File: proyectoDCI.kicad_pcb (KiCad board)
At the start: 2 copper layers, 45 x 20 mm, 27 parts, among them P1 CONN_02X04, P2 CONN_01X01, P3 GSG-RF-CONN, P4 GSG-RF-CONN, U1 AD5933, U2 ADG849, U3 AD8606, U4 ASFLMB-16.000MHZ-LY-T, U5 ADP150

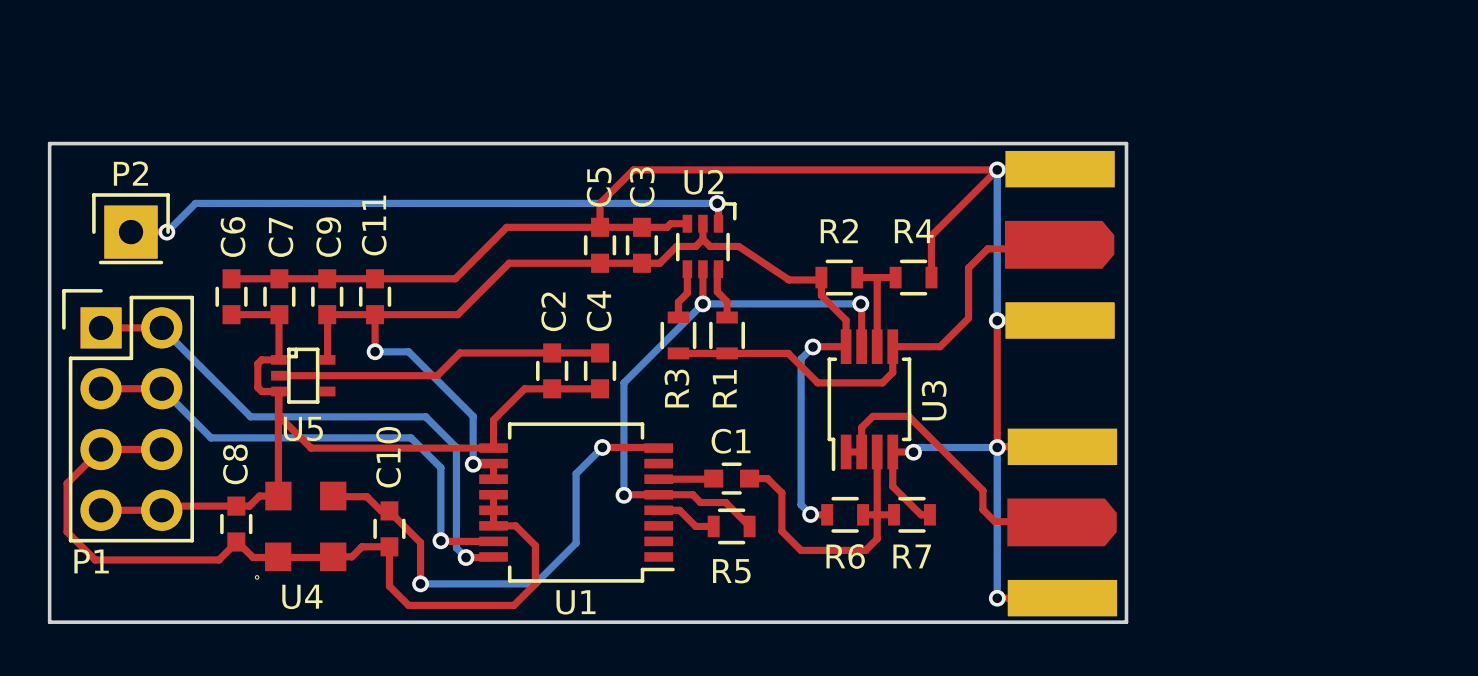
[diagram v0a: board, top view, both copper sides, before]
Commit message: Solucionados todos los problemas de DRC
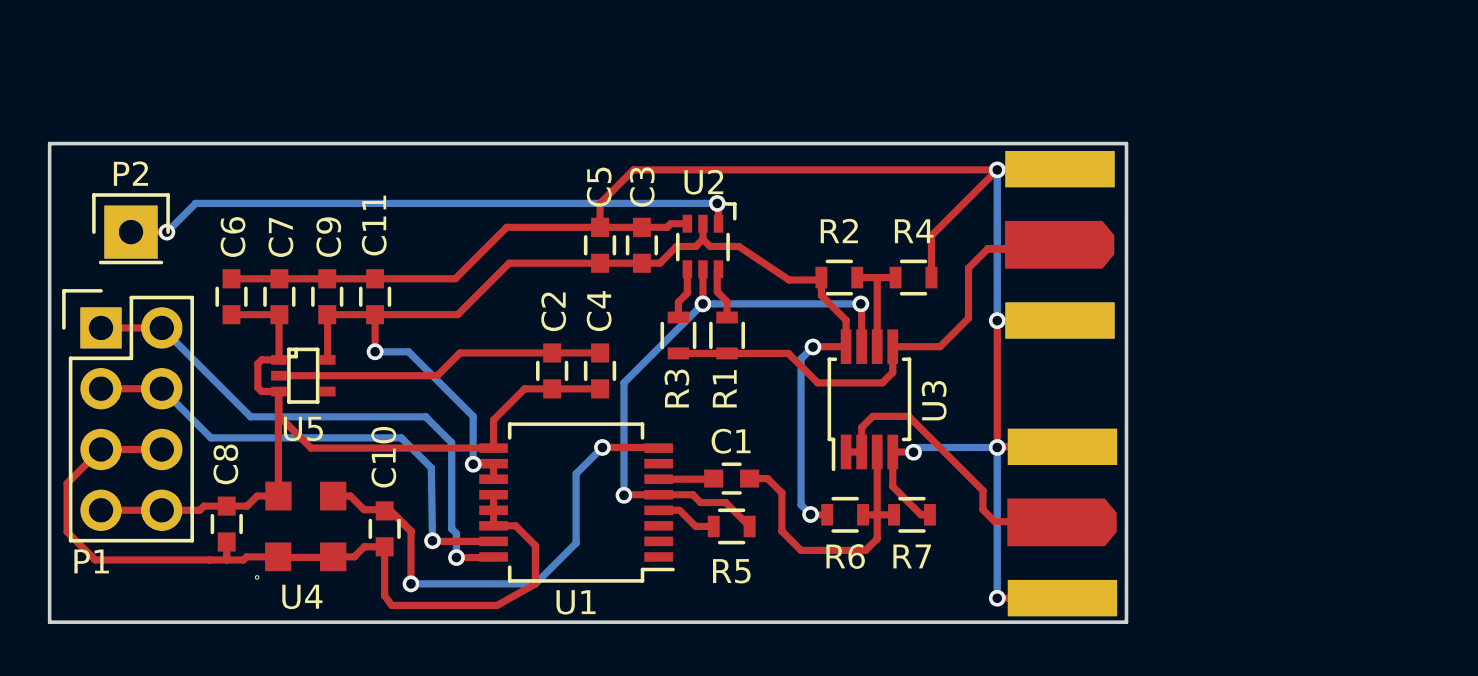
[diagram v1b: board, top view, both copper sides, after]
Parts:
- moved C8 0.40 mm to (157.4, 116.4)
- moved C10 0.20 mm to (164.0, 116.6)
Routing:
- net /Senal/CIN: track 20.6 -> 25.7 mm
- net /Senal/COUT: track 12.3 -> 14.6 mm
- net /Otros/MCLK: track 20.0 -> 22.1 mm
- added copper zone on B.Cu, net GND
- added copper zone on F.Cu, net GND

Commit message: Se agrego la silueta del TCXO y se corrigieron los footprints de los SMA
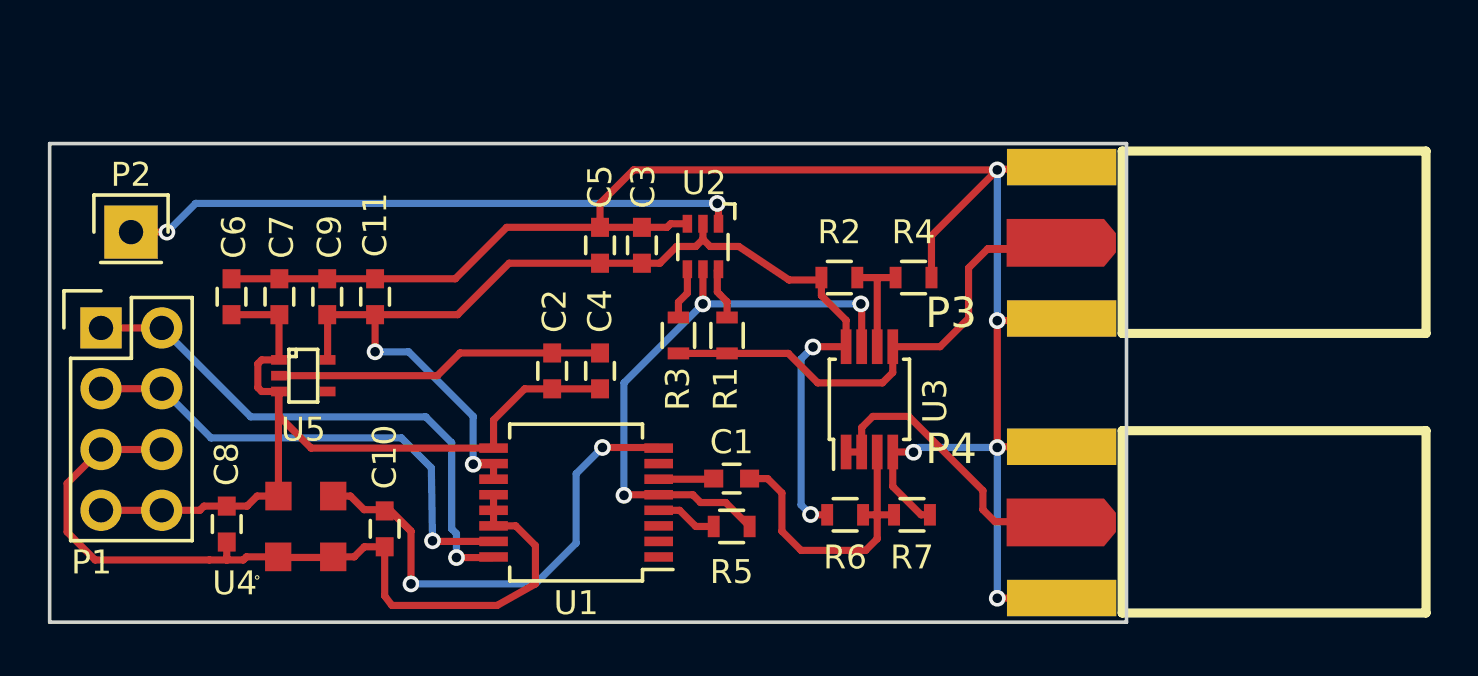
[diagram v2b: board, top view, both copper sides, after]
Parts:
- P3, P4: moved to F.Cu
- moved P3 2.62 mm to (201.2, 103.4)
- moved P4 2.54 mm to (201.2, 115.1)
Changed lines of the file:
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@@
   )
   (setup
-    (last_trace_width 0.3)
+    (last_trace_width 0.15)
     (user_trace_width 0.15)
     (user_trace_width 0.3)
@@
     (add_net VDD)
   )
+  (module SMA_EDGE:SMA_EDGE (layer F.Cu)
+    (at 201.168 115.062)
+    (fp_text reference P4 (at -13.5 -1.8) (layer F.SilkS)
+      (effects (font (thickness 0.3048)))
+    )
+    (fp_text value GSG-RF-CONN (at 0 2.54) (layer F.SilkS) hide
+      (effects (font (thickness 0.3048)))
+    )
+    (fp_line (start -6.35 -2.5654) (end -6.35 5.0546) (layer F.SilkS) (width 0.381))
+    (fp_line (start -6.35 5.0546) (end 6.35 5.0546) (layer F.SilkS) (width 0.381))
+    (fp_line (start 6.35 5.0546) (end 6.35 -2.5654) (layer F.SilkS) (width 0.381))
+    (fp_line (start 6.35 -2.5654) (end -6.35 -2.5654) (layer F.SilkS) (width 0.381))
+    (pad 0 connect rect (at -8.8773 -1.89484) (size 4.572 1.524) (layers *.Cu F.Mask)
+      (net 2 GND))
+    (pad 1 connect trapezoid (at -6.858 1.27) (size 0.50038 1.39954) (rect_delta 0.59944 0 ) (layers F.Cu F.Mask)
+      (net 14 /Senal/COUT))
+    (pad 2 connect rect (at -8.8773 4.42976) (size 4.572 1.524) (layers *.Cu F.Mask)
+      (net 2 GND))
+    (pad 1 connect rect (at -9.144 1.27) (size 4.07162 1.99898) (layers F.Cu F.Mask)
+      (net 14 /Senal/COUT))
+    (model SMA_EDGE.wrl
+      (at (xyz -0.205 -0.05 -0.12))
+      (scale (xyz 1.3 1.3 1.3))
+      (rotate (xyz 270 0 180))
+    )
+  )
+  (module SMA_EDGE:SMA_EDGE (layer F.Cu)
+    (at 201.168 103.378)
+    (fp_text reference P3 (at -13.5 4.2) (layer F.SilkS)
+      (effects (font (thickness 0.3048)))
+    )
+    (fp_text value GSG-RF-CONN (at 0 2.54) (layer F.SilkS) hide
+      (effects (font (thickness 0.3048)))
+    )
+    (fp_line (start -6.35 -2.5654) (end -6.35 5.0546) (layer F.SilkS) (width 0.381))
+    (fp_line (start -6.35 5.0546) (end 6.35 5.0546) (layer F.SilkS) (width 0.381))
+    (fp_line (start 6.35 5.0546) (end 6.35 -2.5654) (layer F.SilkS) (width 0.381))
+    (fp_line (start 6.35 -2.5654) (end -6.35 -2.5654) (layer F.SilkS) (width 0.381))
+    (pad 0 connect rect (at -8.8773 -1.89484) (size 4.572 1.524) (layers *.Cu F.Mask)
+      (net 2 GND))
+    (pad 1 connect trapezoid (at -6.858 1.27) (size 0.50038 1.39954) (rect_delta 0.59944 0 ) (layers F.Cu F.Mask)
+      (net 15 /Senal/CIN))
+    (pad 2 connect rect (at -8.8773 4.42976) (size 4.572 1.524) (layers *.Cu F.Mask)
+      (net 2 GND))
+    (pad 1 connect rect (at -9.144 1.27) (size 4.07162 1.99898) (layers F.Cu F.Mask)
+      (net 15 /Senal/CIN))
+    (model SMA_EDGE.wrl
+      (at (xyz -0.205 -0.05 -0.12))
+      (scale (xyz 1.3 1.3 1.3))
+      (rotate (xyz 270 0 180))
+    )
+  )
+  (module propios:TCXO (layer F.Cu)
+    (at 160.7 116.5)
+    (fp_text reference U4 (at -2.966 2.372) (layer F.SilkS)
+      (effects (font (size 1 1) (thickness 0.15)))
+    )
+    (fp_text value ASFLMB-16.000MHZ-LY-T (at 0.09 2.68) (layer F.Fab)
+      (effects (font (size 1 1) (thickness 0.15)))
+    )
+    (fp_line (start -1.6 0.2) (end -1.6 -2.5) (layer F.CrtYd) (width 0.15))
+    (fp_line (start -1.6 -2.5) (end 1.6 -2.5) (layer F.CrtYd) (width 0.15))
+    (fp_line (start 1.6 -2.5) (end 1.6 2.6) (layer F.CrtYd) (width 0.15))
+    (fp_line (start 1.6 2.6) (end -1.6 2.6) (layer F.CrtYd) (width 0.15))
+    (fp_line (start -1.6 2.6) (end -1.6 0.2) (layer F.CrtYd) (width 0.15))
+    (fp_circle (center -2.03 2.13) (end -2.01 2.13) (layer F.SilkS) (width 0.15))
+    (pad 1 smd rect (at -1.15 1.27) (size 1.1 1.2) (layers F.Cu F.Paste F.Mask)
+      (net 2 GND))
+    (pad 2 smd rect (at 1.15 1.27) (size 1.1 1.2) (layers F.Cu F.Paste F.Mask)
+      (net 2 GND))
+    (pad 4 smd rect (at -1.14 -1.27) (size 1.1 1.2) (layers F.Cu F.Paste F.Mask)
+      (net 1 VDD))
+    (pad 3 smd rect (at 1.15 -1.27) (size 1.1 1.2) (layers F.Cu F.Paste F.Mask)
+      (net 9 /Otros/MCLK))
+  )
   (module Capacitors_SMD:C_0603 (layer F.Cu)
     (at 164 116.6 270)
@@
     )
   )
-  (module propios:TCXO (layer F.Cu)
-    (at 160.7 116.5)
-    (fp_text reference U4 (at -0.16 2.974) (layer F.SilkS)
-      (effects (font (size 1 1) (thickness 0.15)))
-    )
-    (fp_text value ASFLMB-16.000MHZ-LY-T (at 0.09 2.68) (layer F.Fab)
-      (effects (font (size 1 1) (thickness 0.15)))
-    )
-    (fp_circle (center -2.03 2.13) (end -2.01 2.13) (layer F.SilkS) (width 0.15))
-    (pad 1 smd rect (at -1.15 1.27) (size 1.1 1.2) (layers F.Cu F.Paste F.Mask)
-      (net 2 GND))
-    (pad 2 smd rect (at 1.15 1.27) (size 1.1 1.2) (layers F.Cu F.Paste F.Mask)
-      (net 2 GND))
-    (pad 4 smd rect (at -1.14 -1.27) (size 1.1 1.2) (layers F.Cu F.Paste F.Mask)
-      (net 1 VDD))
-    (pad 3 smd rect (at 1.15 -1.27) (size 1.1 1.2) (layers F.Cu F.Paste F.Mask)
-      (net 9 /Otros/MCLK))
-  )
   (module TO_SOT_Packages_SMD:SC-70-5 (layer F.Cu)
     (at 160.6 110.2 270)
@@
       (scale (xyz 1 1 1))
       (rotate (xyz 0 0 90))
-    )
-  )
-  (module SMA_EDGE:SMA_EDGE (layer B.Cu)
-    (at 201.1 106)
-    (fp_text reference P3 (at -13.5 -4.2) (layer B.SilkS)
-      (effects (font (thickness 0.3048)) (justify mirror))
-    )
-    (fp_text value GSG-RF-CONN (at 0 -2.54) (layer B.SilkS) hide
-      (effects (font (thickness 0.3048)) (justify mirror))
-    )
-    (fp_line (start -6.35 2.5654) (end -6.35 -5.0546) (layer B.SilkS) (width 0.381))
-    (fp_line (start -6.35 -5.0546) (end 6.35 -5.0546) (layer B.SilkS) (width 0.381))
-    (fp_line (start 6.35 -5.0546) (end 6.35 2.5654) (layer B.SilkS) (width 0.381))
-    (fp_line (start 6.35 2.5654) (end -6.35 2.5654) (layer B.SilkS) (width 0.381))
-    (pad 0 connect rect (at -8.8773 1.89484) (size 4.572 1.524) (layers *.Cu B.Mask)
-      (net 2 GND))
-    (pad 1 connect trapezoid (at -6.858 -1.27) (size 0.50038 1.39954) (rect_delta 0.59944 0 ) (layers F.Cu B.Mask)
-      (net 15 /Senal/CIN))
-    (pad 2 connect rect (at -8.8773 -4.42976) (size 4.572 1.524) (layers *.Cu B.Mask)
-      (net 2 GND))
-    (pad 1 connect rect (at -9.144 -1.27) (size 4.07162 1.99898) (layers F.Cu B.Mask)
-      (net 15 /Senal/CIN))
-    (model SMA_EDGE.wrl
-      (at (xyz -0.205 -0.05 -0.12))
-      (scale (xyz 1.3 1.3 1.3))
-      (rotate (xyz 270 0 180))
-    )
-  )
-  (module SMA_EDGE:SMA_EDGE (layer B.Cu)
-    (at 201.2 117.6)
-    (fp_text reference P4 (at -13.5 1.8) (layer B.SilkS)
-      (effects (font (thickness 0.3048)) (justify mirror))
-    )
-    (fp_text value GSG-RF-CONN (at 0 -2.54) (layer B.SilkS) hide
-      (effects (font (thickness 0.3048)) (justify mirror))
-    )
-    (fp_line (start -6.35 2.5654) (end -6.35 -5.0546) (layer B.SilkS) (width 0.381))
-    (fp_line (start -6.35 -5.0546) (end 6.35 -5.0546) (layer B.SilkS) (width 0.381))
-    (fp_line (start 6.35 -5.0546) (end 6.35 2.5654) (layer B.SilkS) (width 0.381))
-    (fp_line (start 6.35 2.5654) (end -6.35 2.5654) (layer B.SilkS) (width 0.381))
-    (pad 0 connect rect (at -8.8773 1.89484) (size 4.572 1.524) (layers *.Cu B.Mask)
-      (net 2 GND))
-    (pad 1 connect trapezoid (at -6.858 -1.27) (size 0.50038 1.39954) (rect_delta 0.59944 0 ) (layers F.Cu B.Mask)
-      (net 14 /Senal/COUT))
-    (pad 2 connect rect (at -8.8773 -4.42976) (size 4.572 1.524) (layers *.Cu B.Mask)
-      (net 2 GND))
-    (pad 1 connect rect (at -9.144 -1.27) (size 4.07162 1.99898) (layers F.Cu B.Mask)
-      (net 14 /Senal/COUT))
-    (model SMA_EDGE.wrl
-      (at (xyz -0.205 -0.05 -0.12))
-      (scale (xyz 1.3 1.3 1.3))
-      (rotate (xyz 270 0 180))
     )
   )
@@
   (gr_line (start 195.056 110.73) (end 215.056 110.73) (angle 90) (layer Dwgs.User) (width 0.2))
   (gr_line (start 150 113) (end 141 113) (angle 90) (layer Dwgs.User) (width 0.2))
-  (segment (start 154.686 115.824) (end 156.276 115.824) (width 0.3) (layer F.Cu) (net 1) (status 400000))
-  (segment (start 156.45 115.65) (end 157.4 115.65) (width 0.3) (layer F.Cu) (net 1) (status 800000))
+  (segment (start 154.686 115.824) (end 156.276 115.824) (width 0.3) (layer F.Cu) (net 1))
+  (segment (start 156.45 115.65) (end 157.4 115.65) (width 0.3) (layer F.Cu) (net 1))
   (segment (start 156.276 115.824) (end 156.45 115.65) (width 0.3) (layer F.Cu) (net 1))
-  (segment (start 157.4 115.65) (end 158.25 115.65) (width 0.3) (layer F.Cu) (net 1) (status 400000))
+  (segment (start 157.4 115.65) (end 158.25 115.65) (width 0.3) (layer F.Cu) (net 1))
   (segment (start 158.25 115.65) (end 158.67 115.23) (width 0.3) (layer F.Cu) (net 1))
-  (segment (start 158.67 115.23) (end 159.56 115.23) (width 0.3) (layer F.Cu) (net 1) (status 800000))
+  (segment (start 158.67 115.23) (end 159.56 115.23) (width 0.3) (layer F.Cu) (net 1))
   (segment (start 159.584 110.8604) (end 158.8604 110.8604) (width 0.3) (layer F.Cu) (net 1))
   (segment (start 158.8604 109.5396) (end 159.584 109.5396) (width 0.3) (layer F.Cu) (net 1))
